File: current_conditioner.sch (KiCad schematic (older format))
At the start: 17 parts, among them J1 RJ45, P1 CON, P2 gnd_ref, U1 AD8422, U2 AD8609, U3 AD8609

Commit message: Started building PCB
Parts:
- renumbered U3 to U2
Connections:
- no-connect marks 10 -> 11
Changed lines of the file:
@@
 Sheet 1 1
 Title "Current Conditioner"
-Date "18 may 2014"
+Date "19 may 2014"
 Rev ""
 Comp "Visgene Inc."
@@
 vgnd
 $Comp
-L TL074 U3
+L TL074 U2
 U 3 1 53791DA7
 P 5050 4000
-F 0 "U3" H 5100 4200 60  0000 C CNN
+F 0 "U2" H 5100 4200 60  0000 C CNN
 F 1 "AD8609" H 5200 3800 50  0000 C CNN
 F 2 "" H 5050 4000 60  0000 C CNN
@@
 NoConn ~ 4200 4200
 NoConn ~ 4200 4100
+NoConn ~ 4050 6000
 $EndSCHEMATC

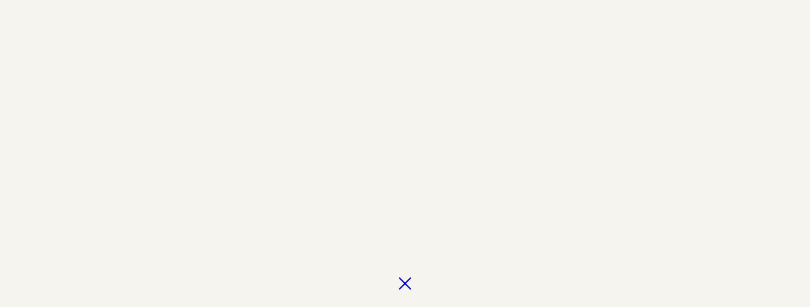
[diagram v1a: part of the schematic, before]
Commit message: removed x on schematic
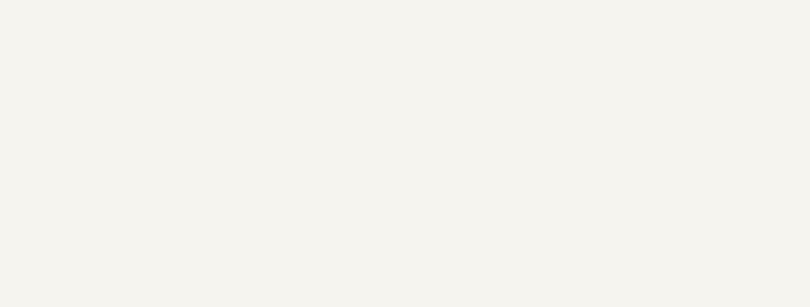
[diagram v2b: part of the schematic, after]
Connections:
- no-connect marks 11 -> 10
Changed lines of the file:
@@
 Sheet 1 1
 Title "Current Conditioner"
-Date "19 may 2014"
+Date "23 may 2014"
 Rev ""
 Comp "Visgene Inc."
@@
 NoConn ~ 4200 4200
 NoConn ~ 4200 4100
-NoConn ~ 4050 6000
 $EndSCHEMATC
